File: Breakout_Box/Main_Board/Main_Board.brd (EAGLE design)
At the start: 60 x 100 mm, 19 parts, among them CN1 19PIN_LEMO

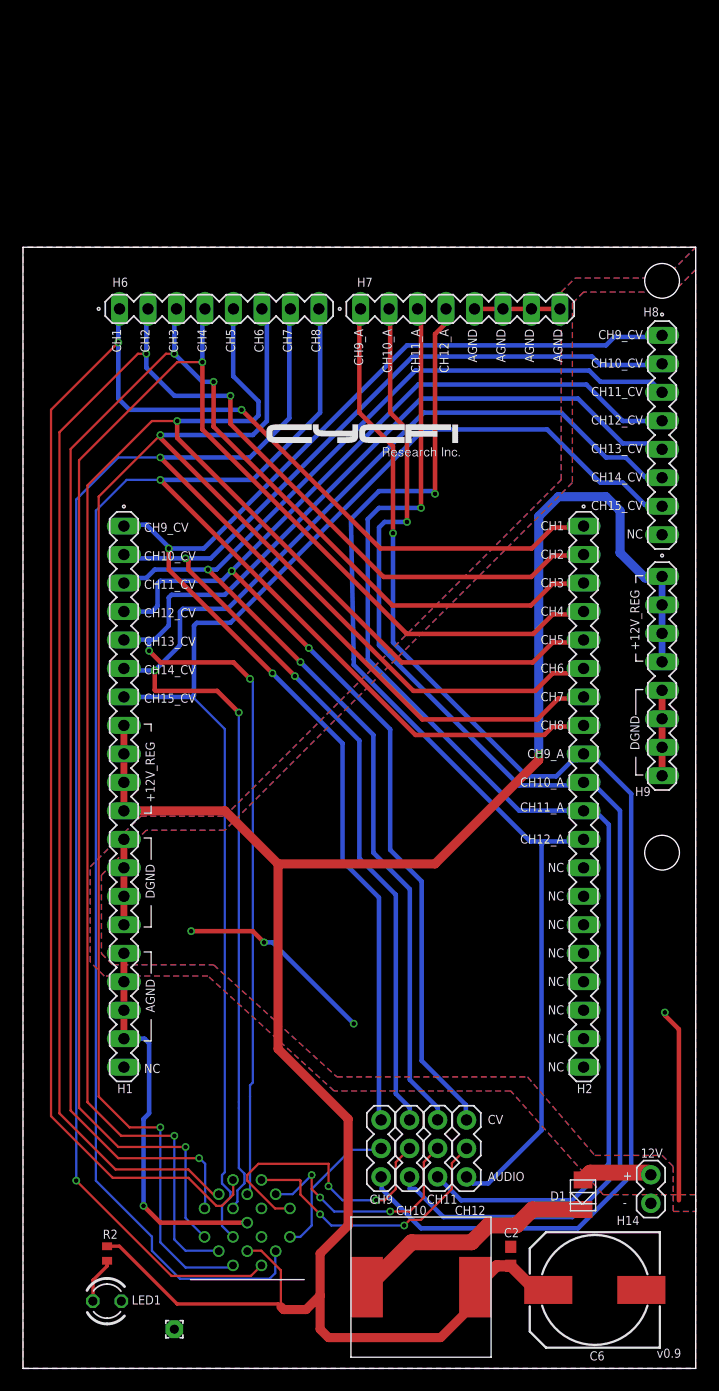
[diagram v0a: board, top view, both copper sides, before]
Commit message: create version 2.1 and update main and midi modules and delete nexyus cad drawings
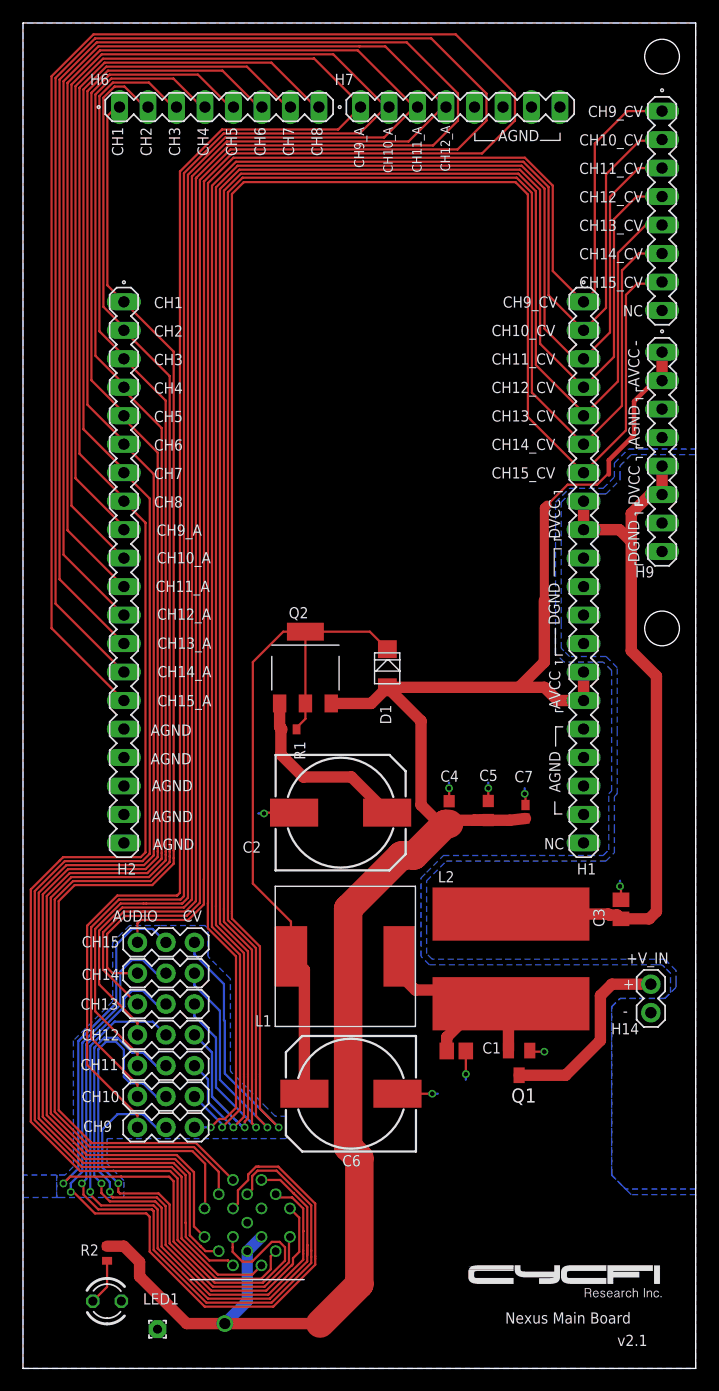
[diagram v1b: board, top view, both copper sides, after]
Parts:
- added C1, C3: 22uF, resistor:C0805
- added C4: 1uF, resistor:C0603
- added C5: 10uF, resistor:C0603
- added C7: 1nF, resistor:C0402K
- added H3, H4, H5: (no value), con-lstb:MA03-1_
- added L2: 82uH, resistor:L1280
- added Q1: DMP3099L, CYCFI_semicon:SOT23
- added Q2: DSS6060, CYCFI_semicon:SOT-223-4
- added R1: 1k, resistor:R0402
- C2: value 0.1uF -> 470uF; device resistor:C0603 -> resistor:140CLH-1010
- D1: value FM4007W -> FM4004W
- L1: value 100uH -> 1mH; device resistor:L1280 -> inductors:SDR
- moved D1 47.3 mm to (32.5, 60.8), turned to 90 degrees
- moved H1 45.6 mm to (50.0, 71.0)
- moved H2 45.6 mm to (9.00, 71.0)
- moved C2 42.4 mm to (28.3, 49.6), turned to 0 degrees
- moved L1 30.2 mm to (43.0, 36.5), turned to 90 degrees
- moved H13 28.7 mm to (12.8, 29.8), turned to 0 degrees
- moved C6 27.9 mm to (29.2, 24.5)
- moved H12 25.3 mm to (12.8, 27.0), turned to 0 degrees
- moved H11 22.2 mm to (12.8, 24.2), turned to 0 degrees
- moved H8 20.0 mm to (57.0, 103.2)
- moved H9 20.0 mm to (57.0, 81.8)
- moved H10 19.3 mm to (12.8, 21.5), turned to 0 degrees
- moved H6 18.0 mm to (17.5, 112.5)
- moved H7 18.0 mm to (39.0, 112.5)
- moved H14 17.0 mm to (56.0, 33.0)
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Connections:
- removed net +12V_REG: C2.1, C6.+, CN1.P$16, H1.10, H1.11, H1.8, H1.9, H9.1, H9.2, H9.3, H9.4, L1.P$2, R2.1
- removed net AGND: C2.2, C6.-, CN1.P$19, GND.1, H1.16, H1.17, H1.18, H1.19, H14.1, H7.5, H7.6, H7.7, H7.8, LED1.K
- removed net DGND: H1.12, H1.13, H1.14, H1.15, H9.5, H9.6, H9.7, H9.8
- removed net N$22: H2.19
- removed net N$23: H2.20
- removed net N$24: H1.20
- removed net N$26 (its old number): CN1.P$18
- removed net N$31: D1.CATHODE, L1.P$1
- removed net N$60: CN1.P$13, H1.5, H8.5
- removed net N$61: CN1.P$14, H1.6, H8.6
- removed net N$62: CN1.P$15, H1.7, H8.7
- removed net N$9 (its old number): CN1.P$17
- new net +AVCC: C4.1, C5.1, C7.1, CN1.P$16, CN1.P$17, D1.ANODE, H1.14, H1.15, H9.1, H9.2, Q2.P$3, R2.1
- new net +DVCC: C3.1, H1.8, H1.9, H9.5, H9.6, L1.P$2
- new net GND: C1.2, C2.-, C3.2, C4.2, C5.2, C6.-, C7.2, CN1.P$18, CN1.P$19, GND.1, H1.10, H1.11, H1.12, H1.13, H1.16, H1.17, H1.18, H1.19, H14.1, H2.16, H2.17, H2.18, H2.19, H2.20, H7.5, H7.6, H7.7, H7.8, H9.3, H9.4, H9.7, H9.8, LED1.K, Q1.1
- new net N$33: H1.5, H3.3, H8.5
- new net N$34: H1.6, H4.3, H8.6
- new net N$35: H1.7, H5.3, H8.7
- new net N$36: CN1.P$13, H3.2
- new net N$37: CN1.P$14, H4.2
- new net N$38: CN1.P$15, H5.2
- net N$1: now also H3.1
- net N$17: now also H5.1
- net N$19: now also C1.1, L1.P$1, L2.P$1, Q1.2; no longer H2.16
- net N$2: now also Q1.3; no longer D1.ANODE
- net N$20: now also C2.+, Q2.P$1, R1.1; no longer H2.17
- net N$21: now also C6.+, D1.CATHODE, L2.P$2, Q2.P$2, Q2.P$4, R1.2; no longer H2.18
- net N$3: now also H4.1
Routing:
- net N$17: track 0.00 -> 208.6 mm
- net N$3: track 0.00 -> 207.4 mm
- net N$1: track 0.00 -> 201.4 mm
- net +12V_REG: track 195.9 -> 0.00 mm, vias 1 -> 0
- net N$35: track 0.00 -> 179.9 mm, vias 0 -> 1
- net N$34: track 0.00 -> 175.0 mm, vias 0 -> 1
- net +AVCC: track 0.00 -> 169.7 mm, vias 0 -> 1
- net N$33: track 0.00 -> 169.7 mm, vias 0 -> 1
- net N$60: track 117.6 -> 0.00 mm, vias 2 -> 0
- net N$61: track 116.7 -> 0.00 mm, vias 2 -> 0
- net N$62: track 114.9 -> 0.00 mm
- net N$28: track 100.4 -> 197.6 mm, vias 1 -> 0
- net N$29: track 110.9 -> 191.9 mm, vias 1 -> 0
- net N$37: track 0.00 -> 72.6 mm, vias 0 -> 1
- net N$18: track 115.3 -> 187.2 mm, vias 1 -> 0
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- added copper zone on layer 16, net GND
- added copper zone on layer 16, net N$22
- added copper zone on layer 16, net N$23
- removed copper zone on layer 1, net AGND
- removed copper zone on layer 16, net AGND
- removed copper zone on layer 1, net DGND
- removed copper zone on layer 16, net DGND
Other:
- board size 60 x 100 mm -> 60 x 120 mm
- board text added: "+V_IN"
- board text added: "AVCC"
- board text added: "CH13"
- board text added: "CH13_A"
- board text added: "CH14"
- board text added: "CH14_A"
- board text added: "CH15"
- board text added: "CH15_A"
- board text added: "DVCC"
- board text added: "L1"
- board text added: "L2"
- board text added: "Nexus Main Board"
- board text added: "Q2"
- board text added: "v2.1"
- board text removed: "+12V_REG"
- board text removed: "12V"
- board text removed: "C2"
- board text removed: "C6"
- board text removed: "D1"
- board text removed: "H1"
- board text removed: "H2"
- board text removed: "H6"
- board text removed: "H7"
- board text removed: "H8"
- board text removed: "H9"
- board text removed: "LED1"
- board text removed: "R2"
- board text removed: "v0.9"
